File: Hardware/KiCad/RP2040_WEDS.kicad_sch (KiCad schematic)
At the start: 73 parts, among them J1 Barrel_Jack_Switch_Pin3Ring, J2 Analog Soil Header, J3 LiPo Batt, J4 I2C Soil Header, J5 Conn_02x05_Odd_Even, J6 SMA-J-P-H-RA-TH1, J7 USB Header, Q1 Q_PMOS_DGS, Q2 Q_PMOS_DGS, SW1 SW_Push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

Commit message: changes
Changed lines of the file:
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@@
     (effects (font (size 2.2606 2.2606)) (justify left bottom))
   )
-  (text "Cap close to pin 44" (at 92.71 71.12 0)
+  (text "Cap close to pin 44" (at 15.24 87.63 0)
     (effects (font (size 1.27 1.27)) (justify left bottom))
   )

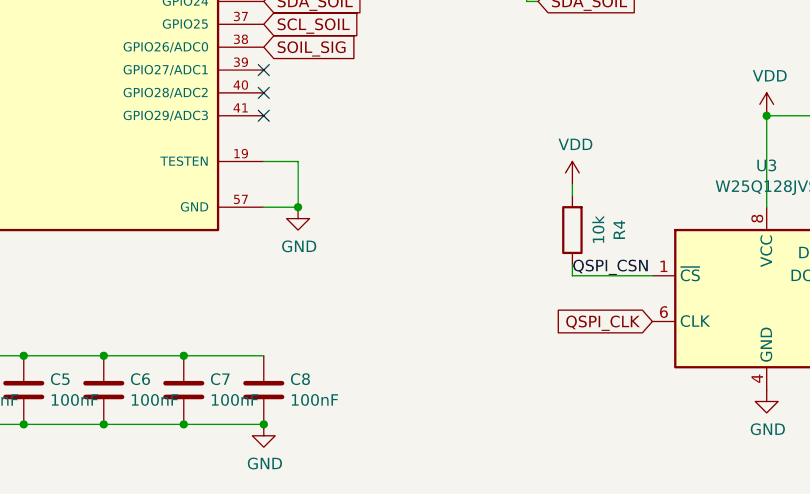
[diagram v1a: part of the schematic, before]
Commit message: Added power fills for 3V3, VDD and VDC
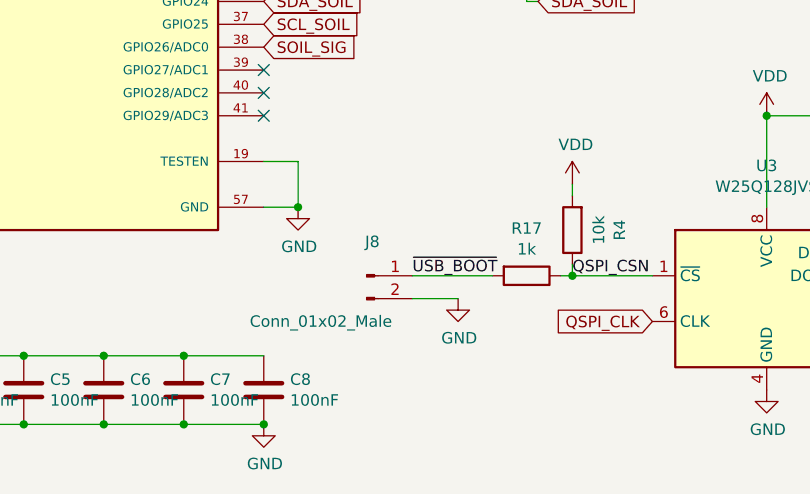
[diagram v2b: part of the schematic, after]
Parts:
- added J8: Conn_01x02_Male, Connector_PinHeader_1.27mm:PinHeader_1x02_P1.27mm_Vertical, symbol Connector:Conn_01x02_Male
- added R17: 1k, Resistor_SMD:R_0603_1608Metric, symbol Device:R
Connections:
- net GND: now also J8.2 (Pin_2)
- net QSPI_CSN: now also R17.1
- new net ~{USB_BOOT}: J8.1 (Pin_1), R17.2
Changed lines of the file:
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@@
   (junction (at 125.73 27.94) (diameter 0) (color 0 0 0 0)
   )
+  (junction (at 115.57 172.72) (diameter 0) (color 0 0 0 0)
+  )
   (junction (at 142.24 21.59) (diameter 0) (color 0 0 0 0)
   )
@@
     (stroke (width 0) (type default) (color 0 0 0 0))
   )
+  (wire (pts (xy 97.79 172.72) (xy 106.68 172.72))
+    (stroke (width 0) (type default) (color 0 0 0 0))
+  )
+  (wire (pts (xy 114.3 172.72) (xy 115.57 172.72))
+    (stroke (width 0) (type default) (color 0 0 0 0))
+  )
   (wire (pts (xy 36.83 181.61) (xy 45.72 181.61))
     (stroke (width 0) (type default) (color 0 0 0 0))
@@
     (stroke (width 0) (type default) (color 0 0 0 0))
   )
+  (wire (pts (xy 97.79 175.26) (xy 102.87 175.26))
+    (stroke (width 0) (type default) (color 0 0 0 0))
+  )
   (wire (pts (xy 220.98 123.19) (xy 220.98 113.03))
     (stroke (width 0) (type default) (color 0 0 0 0))
@@
     (effects (font (size 1.27 1.27)) (justify left bottom))
   )
+  (label "~{USB_BOOT}" (at 97.79 172.72 0)
+    (effects (font (size 1.27 1.27)) (justify left bottom))
+  )
   (global_label "SDA" (shape input) (at 35.56 139.7 180) (fields_autoplaced)
     (effects (font (size 1.27 1.27)) (justify right))
@@
     (pin "2")
   )
+  (symbol (lib_id "Device:R") (at 110.49 172.72 270) (unit 1)
+    (in_bom yes) (on_board yes)
+    (property "Reference" "R17" (id 0) (at 110.49 167.4622 90))
+    (property "Value" "1k" (id 1) (at 110.49 169.7736 90))
+    (property "Footprint" "Resistor_SMD:R_0603_1608Metric" (id 2) (at 110.49 170.942 90)
+      (effects (font (size 1.27 1.27)) hide)
+    )
+    (property "Datasheet" "~" (id 3) (at 110.49 172.72 0)
+      (effects (font (size 1.27 1.27)) hide)
+    )
+    (pin "1")
+    (pin "2")
+  )
   (symbol (lib_id "Jumper:SolderJumper_2_Open") (at 93.98 20.32 0) (unit 1)
     (in_bom yes) (on_board yes)
@@
     (pin "1")
   )
+  (symbol (lib_id "Connector:Conn_01x02_Male") (at 92.71 172.72 0) (unit 1)
+    (in_bom yes) (on_board yes)
+    (property "Reference" "J8" (id 0) (at 93.345 168.944 0))
+    (property "Value" "Conn_01x02_Male" (id 1) (at 87.63 177.8 0))
+    (property "Footprint" "Connector_PinHeader_1.27mm:PinHeader_1x02_P1.27mm_Vertical" (id 2) (at 92.71 172.72 0)
+      (effects (font (size 1.27 1.27)) hide)
+    )
+    (property "Datasheet" "~" (id 3) (at 92.71 172.72 0)
+      (effects (font (size 1.27 1.27)) hide)
+    )
+    (pin "1")
+    (pin "2")
+  )
   (symbol (lib_id "power:GND") (at 93.98 72.39 0) (unit 1)
     (in_bom yes) (on_board yes)
@@
     (pin "4")
   )
+  (symbol (lib_id "power:GND") (at 102.87 175.26 0) (unit 1)
+    (in_bom yes) (on_board yes)
+    (property "Reference" "#PWR063" (id 0) (at 102.87 181.61 0)
+      (effects (font (size 1.27 1.27)) hide)
+    )
+    (property "Value" "GND" (id 1) (at 102.997 179.6542 0))
+    (property "Footprint" "" (id 2) (at 102.87 175.26 0)
+      (effects (font (size 1.27 1.27)) hide)
+    )
+    (property "Datasheet" "" (id 3) (at 102.87 175.26 0)
+      (effects (font (size 1.27 1.27)) hide)
+    )
+    (pin "1")
+  )
   (sheet_instances
     (path "/" (page "1"))
@@
       (reference "#PWR062") (unit 1) (value "VDD") (footprint "")
     )
+    (path "/eecf1982-383e-4023-90de-4cf1c40c872f"
+      (reference "#PWR063") (unit 1) (value "GND") (footprint "")
+    )
     (path "/00000000-0000-0000-0000-0000629136f6"
       (reference "#PWR0101") (unit 1) (value "VDD") (footprint "")
@@
       (reference "J7") (unit 1) (value "USB Header") (footprint "Connector_PinHeader_1.27mm:PinHeader_1x04_P1.27mm_Vertical")
     )
+    (path "/87f53324-fd34-468e-b98f-06d9b31382af"
+      (reference "J8") (unit 1) (value "Conn_01x02_Male") (footprint "Connector_PinHeader_1.27mm:PinHeader_1x02_P1.27mm_Vertical")
+    )
     (path "/00000000-0000-0000-0000-00006286e8a9"
       (reference "JP1") (unit 1) (value "SolderJumper_2_Open") (footprint "Jumper:SolderJumper-2_P1.3mm_Open_RoundedPad1.0x1.5mm")
@@
       (reference "R16") (unit 1) (value "27.4") (footprint "Resistor_SMD:R_0603_1608Metric")
     )
+    (path "/3ef5a64e-2eb7-4736-81b9-50572180eda2"
+      (reference "R17") (unit 1) (value "1k") (footprint "Resistor_SMD:R_0603_1608Metric")
+    )
     (path "/00000000-0000-0000-0000-0000624512d3"

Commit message: Updated filepaths
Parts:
- U1: footprint RP2040KICAD:QFN40P700X700X90-57N -> 54-00125:QFN40P700X700X90-57N
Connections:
- no-connect marks 22 -> 41
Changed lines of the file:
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@@
   (no_connect (at 35.56 149.86))
   (no_connect (at 81.28 134.62))
+  (no_connect (at 228.6 77.47))
+  (no_connect (at 223.52 77.47))
+  (no_connect (at 220.98 77.47))
+  (no_connect (at 218.44 77.47))
+  (no_connect (at 215.9 77.47))
+  (no_connect (at 215.9 113.03))
+  (no_connect (at 223.52 113.03))
+  (no_connect (at 226.06 113.03))
+  (no_connect (at 228.6 113.03))
+  (no_connect (at 231.14 113.03))
+  (no_connect (at 205.74 100.33))
+  (no_connect (at 205.74 102.87))
+  (no_connect (at 241.3 87.63))
+  (no_connect (at 241.3 90.17))
+  (no_connect (at 241.3 92.71))
+  (no_connect (at 241.3 95.25))
+  (no_connect (at 205.74 92.71))
+  (no_connect (at 205.74 95.25))
+  (no_connect (at 205.74 97.79))
   (no_connect (at 81.28 149.86))
   (no_connect (at 81.28 129.54))
@@
     (property "Reference" "U1" (id 0) (at 58.42 69.4182 0))
     (property "Value" "RP2040" (id 1) (at 58.42 71.7296 0))
-    (property "Footprint" "RP2040KICAD:QFN40P700X700X90-57N" (id 2) (at 58.42 121.92 0)
+    (property "Footprint" "54-00125:QFN40P700X700X90-57N" (id 2) (at 58.42 121.92 0)
       (effects (font (size 1.27 1.27)) (justify left bottom) hide)
     )
@@
     )
     (path "/00000000-0000-0000-0000-000062224b2d"
-      (reference "U1") (unit 1) (value "RP2040") (footprint "RP2040KICAD:QFN40P700X700X90-57N")
+      (reference "U1") (unit 1) (value "RP2040") (footprint "54-00125:QFN40P700X700X90-57N")
     )
     (path "/00000000-0000-0000-0000-000062062cc0"
